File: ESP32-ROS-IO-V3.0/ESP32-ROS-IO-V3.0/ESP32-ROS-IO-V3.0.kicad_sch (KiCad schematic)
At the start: 47 parts, among them J1 Conn_01x19_Socket, J12 XT60-M, J13 XT60-M, J2 Conn_01x19_Socket, J3 Conn_01x19_Socket, J4 Conn_01x19_Socket, J5 Conn_01x02_Pin, J6 Conn_01x02_Pin, SW1 SW1, SW2 SW2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

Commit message: 一応コピーとって、配置変え開始
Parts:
- J5, J6: footprint (none) -> Connector_PinSocket_2.54mm:PinSocket_1x19_P2.54mm_Vertical
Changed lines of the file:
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@@
 			)
 		)
-		(property "Footprint" ""
+		(property "Footprint" "Connector_PinSocket_2.54mm:PinSocket_1x19_P2.54mm_Vertical"
 			(at 71.12 234.95 0)
 			(effects
@@
 			)
 		)
-		(property "Footprint" ""
+		(property "Footprint" "Connector_PinSocket_2.54mm:PinSocket_1x19_P2.54mm_Vertical"
 			(at 71.12 219.71 0)
 			(effects

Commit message: 名前変更、整理
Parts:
- J12, J13: footprint Connector_AMASS:AMASS_XT60-M_1x02_P7.20mm_Vertical -> XT60PW-M (2):AMASS_XT30PW-F
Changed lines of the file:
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@@
 			)
 		)
-		(property "Footprint" "Connector_AMASS:AMASS_XT60-M_1x02_P7.20mm_Vertical"
+		(property "Footprint" "XT60PW-M (2):AMASS_XT30PW-F"
 			(at 229.87 64.77 0)
 			(effects
@@
 			)
 		)
-		(property "Footprint" "Connector_AMASS:AMASS_XT60-M_1x02_P7.20mm_Vertical"
+		(property "Footprint" "XT60PW-M (2):AMASS_XT30PW-F"
 			(at 227.33 134.62 0)
 			(effects

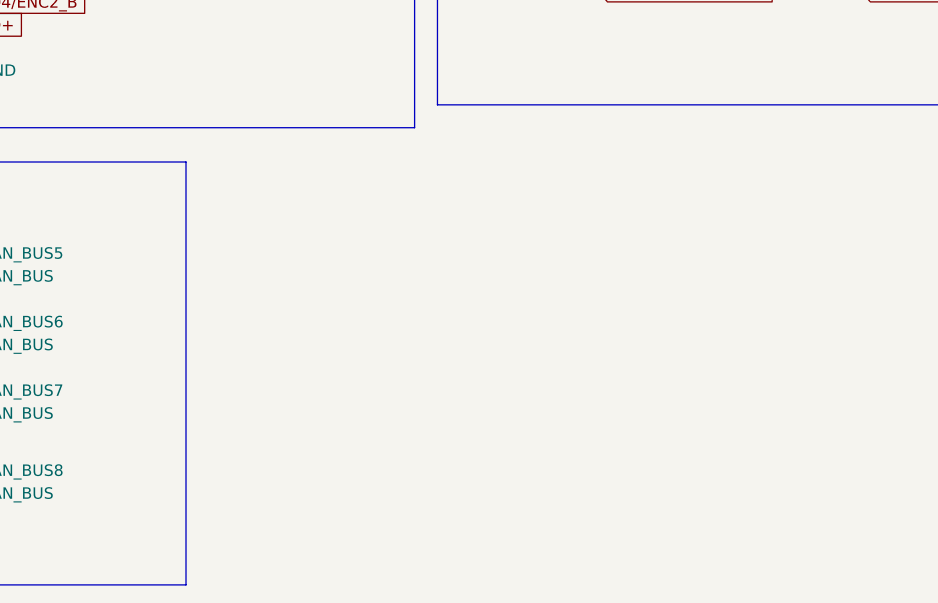
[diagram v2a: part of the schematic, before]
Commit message: 外付けシリアル用の回路を追加（ピン未割り当て）
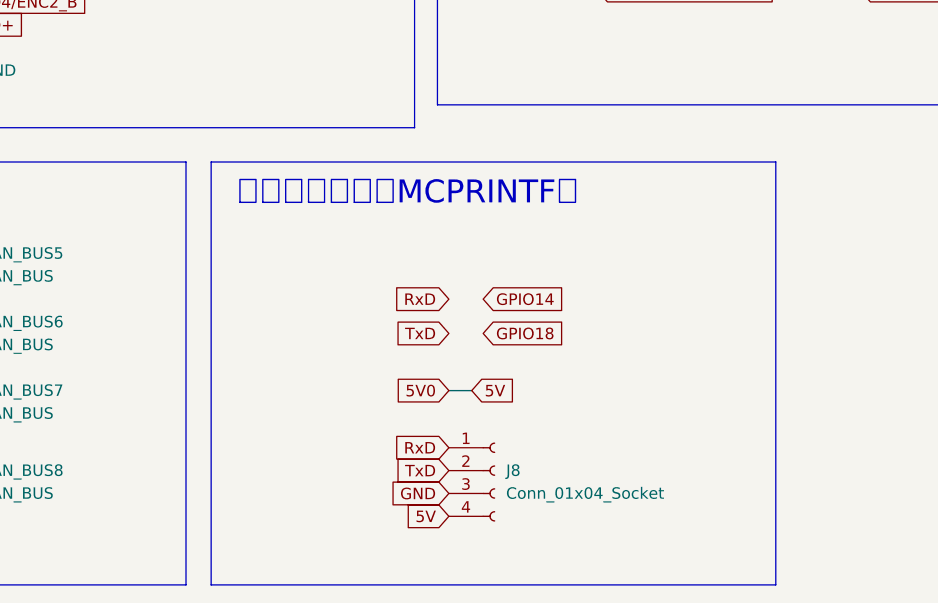
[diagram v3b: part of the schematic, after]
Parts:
- added J8: Conn_01x04_Socket, symbol Connector:Conn_01x04_Socket
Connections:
- net GND: now also J8.3 (Pin_3)
- net 5V0 renamed 5V
- net 5V: now also J8.4 (Pin_4)
- new net RxD: J8.1 (Pin_1)
- new net TxD: J8.2 (Pin_2)
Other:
- note added: "外部シリアル（MCPRINTF）"

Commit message: 外部シリアルにピンを割り当て
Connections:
- net RxD is gone; now on net GPIO14: J8.1 (Pin_1)
- net TxD is gone; now on net GPIO18: J8.2 (Pin_2)
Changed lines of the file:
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@@
+	(wire
+		(pts
+			(xy 250.19 218.44) (xy 254 218.44)
+		)
+		(stroke
+			(width 0)
+			(type default)
+		)
+	)
 	(wire
 		(pts
@@
 		)
 		(stroke
+			(width 0)
+			(type default)
+		)
+	)
+	(wire
+		(pts
+			(xy 250.19 214.63) (xy 254 214.63)
+		)
+		(stroke

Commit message: 割り当てした
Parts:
- J12, J13: footprint XT60PW-M (2):AMASS_XT30PW-F -> XT30PW-F:AMASS_XT30PW-F
- J8: footprint (none) -> Connector_PinSocket_2.54mm:PinSocket_1x19_P2.54mm_Vertical
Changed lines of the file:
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@@
 			)
 		)
-		(property "Footprint" "XT60PW-M (2):AMASS_XT30PW-F"
+		(property "Footprint" "XT30PW-F:AMASS_XT30PW-F"
 			(at 229.87 64.77 0)
 			(effects
@@
 			)
 		)
-		(property "Footprint" ""
+		(property "Footprint" "Connector_PinSocket_2.54mm:PinSocket_1x19_P2.54mm_Vertical"
 			(at 255.27 233.68 0)
 			(effects
@@
 			)
 		)
-		(property "Footprint" "XT60PW-M (2):AMASS_XT30PW-F"
+		(property "Footprint" "XT30PW-F:AMASS_XT30PW-F"
 			(at 227.33 134.62 0)
 			(effects

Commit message: XT30UPB-Mのフットプリントが入らん
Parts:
- added J8, J9: XT30UPB-M, XT30UPB-M:AMASS_XT30UPB-M, symbol XT30UPB-M:XT30UPB-M
- J5, J6: footprint Connector_PinSocket_2.54mm:PinSocket_1x19_P2.54mm_Vertical -> Connector_PinHeader_2.54mm:PinHeader_1x02_P2.54mm_Vertical
- J7: renamed from J8; footprint Connector_PinSocket_2.54mm:PinSocket_1x19_P2.54mm_Vertical -> Connector_PinSocket_2.54mm:PinSocket_1x04_P2.54mm_Vertical

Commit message: フットプリント割り当て
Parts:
- J12, J13: footprint XT30PW-F:AMASS_XT30PW-F -> XT60-M:AMASS_XT60-M
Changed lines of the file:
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@@
 			)
 		)
-		(property "Footprint" "XT30PW-F:AMASS_XT30PW-F"
+		(property "Footprint" "XT60-M:AMASS_XT60-M"
 			(at 229.87 64.77 0)
 			(effects
@@
 			)
 		)
-		(property "Footprint" "XT30PW-F:AMASS_XT30PW-F"
+		(property "Footprint" "XT60-M:AMASS_XT60-M"
 			(at 227.33 134.62 0)
 			(effects

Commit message: たすけてたしろさん
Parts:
- removed VMD1/VMD2: VMD1/VMD2, Connector_PinHeader_2.54mm:PinHeader_1x11_P2.54mm_Vertical, symbol Connector:Conn_01x11_Pin
- removed VMD3/VMD4: VMD3/VMD4, Connector_PinHeader_2.54mm:PinHeader_1x11_P2.54mm_Vertical, symbol Connector:Conn_01x11_Pin
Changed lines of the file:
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@@
-	)
-	(symbol
-		(lib_id "Connector:Conn_01x11_Pin")
-		(at 290.83 167.64 0)
-		(unit 1)
-		(exclude_from_sim no)
-		(in_bom yes)
-		(on_board yes)
-		(dnp no)
-		(fields_autoplaced yes)
-		(property "Reference" "VMD3/VMD4"
-			(at 291.465 149.86 0)
-			(effects
-				(font
-					(size 1.27 1.27)
-				)
-			)
-		)
-		(property "Value" "VMD3/VMD4"
-			(at 291.465 152.4 0)
-			(effects
-				(font
-					(size 1.27 1.27)
-				)
-			)
-		)
-		(property "Footprint" "Connector_PinHeader_2.54mm:PinHeader_1x11_P2.54mm_Vertical"
-			(at 290.83 167.64 0)
-			(effects
-				(font
-					(size 1.27 1.27)
-				)
-				(hide yes)
-			)
-		)
-		(property "Datasheet" "~"
-			(at 290.83 167.64 0)
-			(effects
-				(font
-					(size 1.27 1.27)
-				)
-				(hide yes)
-			)
-		)
-		(property "Description" "Generic connector, single row, 01x11, script generated"
-			(at 290.83 167.64 0)
-			(effects
-				(font
-					(size 1.27 1.27)
-				)
-				(hide yes)
-			)
-		)
-		(pin "7"
-		)
-		(pin "11"
-		)
-		(pin "10"
-		)
-		(pin "1"
-		)
-		(pin "9"
-		)
-		(pin "2"
-		)
-		(pin "6"
-		)
-		(pin "5"
-		)
-		(pin "8"
-		)
-		(pin "4"
-		)
-		(pin "3"
-		)
-		(instances
-			(project "ESP32-ROS-IO-V1.1"
-				(path "/a044ed2e-2600-443c-a3c9-c74abc48d2d6"
-					(reference "VMD3/VMD4")
-					(unit 1)
-				)
-			)
-		)
 	)
 	(symbol
@@
 					(unit 1)
 				)
-			)
-		)
-	)
-	(symbol
-		(lib_id "Connector:Conn_01x11_Pin")
-		(at 261.62 167.64 0)
-		(unit 1)
-		(exclude_from_sim no)
-		(in_bom yes)
-		(on_board yes)
-		(dnp no)
-		(fields_autoplaced yes)
-		(property "Reference" "VMD1/VMD2"
-			(at 262.255 149.86 0)
-			(effects
-				(font
-					(size 1.27 1.27)
-				)
-			)
-		)
-		(property "Value" "VMD1/VMD2"
-			(at 262.255 152.4 0)
-			(effects
-				(font
-					(size 1.27 1.27)
-				)
-			)
-		)
-		(property "Footprint" "Connector_PinHeader_2.54mm:PinHeader_1x11_P2.54mm_Vertical"
-			(at 261.62 167.64 0)
-			(effects
-				(font
-					(size 1.27 1.27)
-				)
-				(hide yes)
-			)
-		)
-		(property "Datasheet" "~"
-			(at 261.62 167.64 0)
-			(effects
-				(font
-					(size 1.27 1.27)
-				)
-				(hide yes)
-			)
-		)
-		(property "Description" "Generic connector, single row, 01x11, script generated"
-			(at 261.62 167.64 0)
-			(effects
-				(font
-					(size 1.27 1.27)
-				)
-				(hide yes)
-			)
-		)
-		(pin "7"
-		)
-		(pin "11"
-		)
-		(pin "10"
-		)
-		(pin "1"
-		)
-		(pin "9"
-		)
-		(pin "2"
-		)
-		(pin "6"
-		)
-		(pin "5"
-		)
-		(pin "8"
-		)
-		(pin "4"
-		)
-		(pin "3"
-		)
-		(instances
-			(project "ESP32-ROS-IO-V1.1"
-				(path "/a044ed2e-2600-443c-a3c9-c74abc48d2d6"
-					(reference "VMD1/VMD2")
-					(unit 1)
-				)
